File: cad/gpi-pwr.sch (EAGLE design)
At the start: 103 parts, among them CN1 HEADER-1X2, CN2 HEADER-3X1, CN3 HEADER-1X2.4, Q1 MOSFETTO247REV, Q3 MOSFETTO247REV, Q5 MOSFETTO247REV, Q6 MOSFETTO247REV, Q7 MOSFETTO247REV, Q8 MOSFETTO247REV, U1 ACS709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

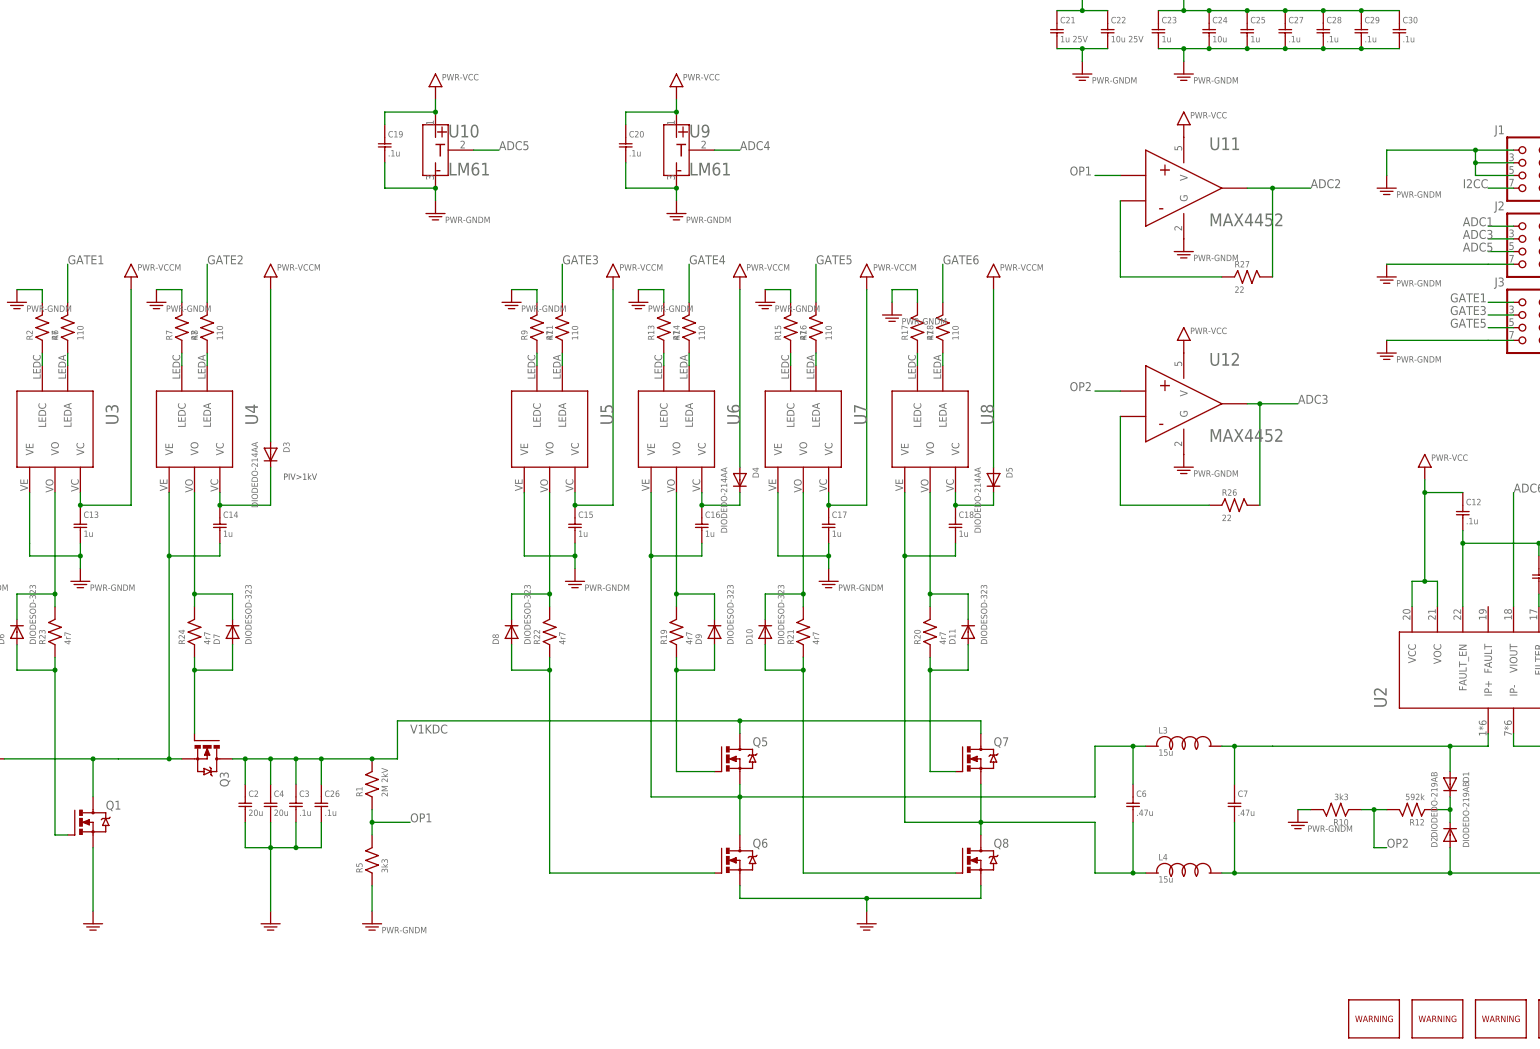
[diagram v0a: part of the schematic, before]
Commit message: output filter
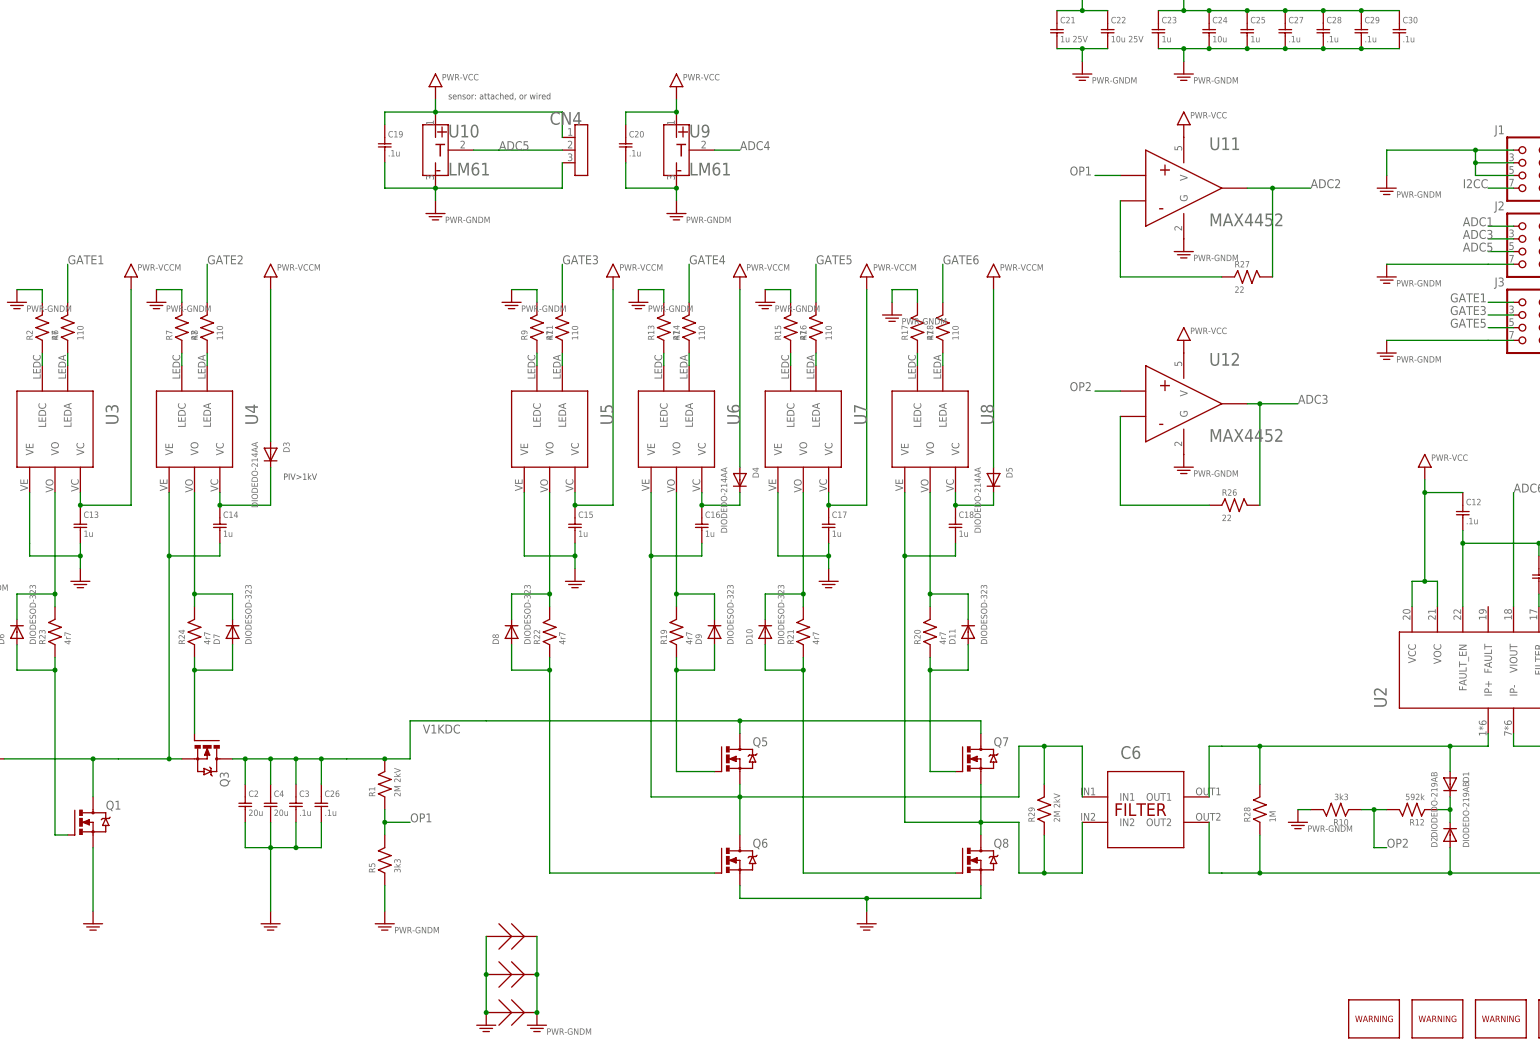
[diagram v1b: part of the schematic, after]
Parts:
- removed C7: .47u, jaw:CR46KI333000N1M
- removed L3, L4: 15u, jaw:L2303
- added CN4: HEADER-3X12MM, jaw:HEADER-3X12MM
- added R28: 1M, jaw:R1206
- added R29: 2M 2kV, jaw:R2512
- added Z1, Z2, Z3: SHORT, jaw:SHORT
- C6: value .47u -> FILTER; device jaw:CR46KI333000N1M -> jaw-brd:FILTER
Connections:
- net ADC5: now also CN4.2
- net GND: now also C13.P$2, C15.P$2, C17.P$2, U3.VE, U5.VE, U7.VE, Z1.P$1, Z2.P$1, Z3.P$1
- net GNDM: now also CN4.3, Z1.P$2, Z2.P$2, Z3.P$2; no longer C13.P$2, C15.P$2, C17.P$2, U3.VE, U5.VE, U7.VE
- net N$15: now also C6.IN1, R29.P$2; no longer C6.P$1, L3.P$1
- net N$16: now also C6.IN2, R29.P$1; no longer C6.P$2, L4.P$1
- net N$24: now also C6.OUT1, R28.P$2; no longer C7.P$1, L3.P$2
- net N$25: now also C6.OUT2, R28.P$1; no longer C7.P$2, L4.P$2
- net VCC: now also CN4.1
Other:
- note added: "sensor: attached, or wired"
- moved on the sheet: R1, R5

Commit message: tweak
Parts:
- removed R29: 2M 2kV, jaw:R2512
- removed R3: 392k, jaw:R1206
- R4: value 392k -> 1M
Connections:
- net ADC1: now also J3.P$1; no longer J2.P$1
- net ADC2: now also J3.P$2; no longer J2.P$2
- net ADC3: now also J3.P$3; no longer J2.P$3
- net ADC4: now also J3.P$4; no longer J2.P$4
- net ADC5: now also J3.P$5; no longer J2.P$5
- net ADC6: now also J3.P$6; no longer J2.P$6
- net GATE1: now also J2.P$1; no longer J3.P$1
- net GATE2: now also J2.P$2; no longer J3.P$2
- net GATE3: now also J2.P$3; no longer J3.P$3
- net GATE4: now also J2.P$4; no longer J3.P$4
- net GATE5: now also J2.P$5; no longer J3.P$5
- net GATE6: now also J2.P$6; no longer J3.P$6
- net N$11: no longer R3.P$2
- net N$15: no longer R29.P$2
- net N$16: no longer R29.P$1
- net N$25: no longer R3.P$1
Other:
- moved on the sheet: J2, J3
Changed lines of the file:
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@@
 <part name="VCC3" library="jaw" deviceset="PWR-VCC" device=""/>
 <part name="J1" library="jaw" deviceset="HEADER-2X4" device=""/>
+<part name="J3" library="jaw" deviceset="HEADER-2X4" device=""/>
 <part name="J2" library="jaw" deviceset="HEADER-2X4" device=""/>
-<part name="J3" library="jaw" deviceset="HEADER-2X4" device=""/>
 <part name="CN3" library="jaw" deviceset="HEADER-1X2" device=".4"/>
 <part name="JP1" library="adafruit" deviceset="PINHD-1X1" device=""/>
@@
 <part name="VCC4" library="jaw" deviceset="PWR-VCC" device=""/>
 <part name="VCC5" library="jaw" deviceset="PWR-VCC" device=""/>
-<part name="R3" library="jaw" deviceset="R" device="1206" value="392k"/>
-<part name="R4" library="jaw" deviceset="R" device="1206" value="392k"/>
+<part name="R4" library="jaw" deviceset="R" device="1206" value="1M"/>
 <part name="R19" library="jaw" deviceset="R" device="SMD0508" value="4r7"/>
 <part name="R20" library="jaw" deviceset="R" device="SMD0508" value="4r7"/>
@@
 <part name="Z3" library="jaw" deviceset="SHORT" device=""/>
 <part name="C6" library="jaw-brd" deviceset="FILTER" device=""/>
-<part name="R29" library="jaw" deviceset="R" device="2512" value="2M 2kV"/>
 </parts>
 <sheets>
@@
 <instance part="VCC3" gate="G$1" x="401.32" y="218.44"/>
 <instance part="J1" gate="A" x="373.38" y="213.36"/>
-<instance part="J2" gate="A" x="373.38" y="198.12"/>
-<instance part="J3" gate="A" x="373.38" y="182.88"/>
+<instance part="J3" gate="A" x="373.38" y="198.12"/>
+<instance part="J2" gate="A" x="373.38" y="182.88"/>
 <instance part="CN3" gate="G$1" x="15.24" y="71.12" rot="R180"/>
 <instance part="JP1" gate="G$1" x="391.16" y="86.36" rot="R180"/>
@@
 <instance part="VCC4" gate="G$1" x="154.94" y="231.14"/>
 <instance part="VCC5" gate="G$1" x="203.2" y="231.14"/>
-<instance part="R3" gate="G$1" x="401.32" y="81.28" rot="R90"/>
 <instance part="R4" gate="G$1" x="401.32" y="91.44" rot="R90"/>
 <instance part="R19" gate="G$1" x="203.2" y="121.92" rot="R90"/>
@@
 <instance part="Z3" gate="G$1" x="170.18" y="60.96"/>
 <instance part="C6" gate="G$1" x="297.18" y="86.36"/>
-<instance part="R29" gate="G$1" x="276.86" y="86.36" rot="R90"/>
 </instances>
 <busses>
@@
 <net name="ADC2" class="0">
 <segment>
-<pinref part="J2" gate="A" pin="P$2"/>
+<pinref part="J3" gate="A" pin="P$2"/>
 <wire x1="378.46" y1="203.2" x2="388.62" y2="203.2" width="0.1524" layer="91"/>
 <label x="388.62" y="203.2" size="1.778" layer="95"/>
@@
 <wire x1="358.14" y1="78.74" x2="358.14" y2="73.66" width="0.1524" layer="91"/>
 <junction x="358.14" y="73.66"/>
-<pinref part="R3" gate="G$1" pin="P$1"/>
-<wire x1="401.32" y1="76.2" x2="401.32" y2="73.66" width="0.1524" layer="91"/>
-<junction x="401.32" y="73.66"/>
 <wire x1="309.88" y1="73.66" x2="312.42" y2="73.66" width="0.1524" layer="91"/>
 <wire x1="312.42" y1="73.66" x2="320.04" y2="73.66" width="0.1524" layer="91"/>
@@
 </segment>
 <segment>
-<pinref part="J2" gate="A" pin="P$1"/>
+<pinref part="J3" gate="A" pin="P$1"/>
 <wire x1="370.84" y1="203.2" x2="365.76" y2="203.2" width="0.1524" layer="91"/>
 <label x="360.68" y="203.2" size="1.778" layer="95"/>
@@
 <net name="ADC4" class="0">
 <segment>
-<pinref part="J2" gate="A" pin="P$4"/>
+<pinref part="J3" gate="A" pin="P$4"/>
 <wire x1="378.46" y1="200.66" x2="388.62" y2="200.66" width="0.1524" layer="91"/>
 <label x="388.62" y="200.66" size="1.778" layer="95"/>
@@
 <wire x1="215.9" y1="88.9" x2="215.9" y2="91.44" width="0.1524" layer="91"/>
 <wire x1="215.9" y1="88.9" x2="271.78" y2="88.9" width="0.1524" layer="91"/>
-<wire x1="271.78" y1="88.9" x2="271.78" y2="99.06" width="0.1524" layer="91"/>
 <junction x="215.9" y="88.9"/>
 <wire x1="198.12" y1="137.16" x2="198.12" y2="88.9" width="0.1524" layer="91"/>
@@
 <junction x="198.12" y="137.16"/>
 <pinref part="C6" gate="G$1" pin="IN1"/>
-<wire x1="271.78" y1="99.06" x2="276.86" y2="99.06" width="0.1524" layer="91"/>
-<wire x1="276.86" y1="99.06" x2="284.48" y2="99.06" width="0.1524" layer="91"/>
-<wire x1="284.48" y1="99.06" x2="284.48" y2="88.9" width="0.1524" layer="91"/>
-<wire x1="276.86" y1="91.44" x2="276.86" y2="99.06" width="0.1524" layer="91"/>
-<junction x="276.86" y="99.06"/>
-<pinref part="R29" gate="G$1" pin="P$2"/>
+<wire x1="271.78" y1="88.9" x2="276.86" y2="88.9" width="0.1524" layer="91"/>
+<wire x1="276.86" y1="88.9" x2="284.48" y2="88.9" width="0.1524" layer="91"/>
 </segment>
 </net>
@@
 <wire x1="264.16" y1="83.82" x2="264.16" y2="91.44" width="0.1524" layer="91"/>
 <wire x1="264.16" y1="83.82" x2="271.78" y2="83.82" width="0.1524" layer="91"/>
-<wire x1="271.78" y1="83.82" x2="271.78" y2="73.66" width="0.1524" layer="91"/>
 <junction x="264.16" y="83.82"/>
 <wire x1="248.92" y1="137.16" x2="248.92" y2="83.82" width="0.1524" layer="91"/>
@@
 <junction x="248.92" y="137.16"/>
 <pinref part="C6" gate="G$1" pin="IN2"/>
-<wire x1="271.78" y1="73.66" x2="276.86" y2="73.66" width="0.1524" layer="91"/>
-<wire x1="276.86" y1="73.66" x2="284.48" y2="73.66" width="0.1524" layer="91"/>
-<wire x1="284.48" y1="73.66" x2="284.48" y2="83.82" width="0.1524" layer="91"/>
-<wire x1="276.86" y1="81.28" x2="276.86" y2="73.66" width="0.1524" layer="91"/>
-<junction x="276.86" y="73.66"/>
-<pinref part="R29" gate="G$1" pin="P$1"/>
+<wire x1="271.78" y1="83.82" x2="276.86" y2="83.82" width="0.1524" layer="91"/>
+<wire x1="276.86" y1="83.82" x2="284.48" y2="83.82" width="0.1524" layer="91"/>
 </segment>
 </net>
@@
 </segment>
 <segment>
-<pinref part="J3" gate="A" pin="P$1"/>
+<pinref part="J2" gate="A" pin="P$1"/>
 <wire x1="370.84" y1="187.96" x2="365.76" y2="187.96" width="0.1524" layer="91"/>
 <label x="358.14" y="187.96" size="1.778" layer="95"/>
@@
 </segment>
 <segment>
-<pinref part="J3" gate="A" pin="P$2"/>
+<pinref part="J2" gate="A" pin="P$2"/>
 <wire x1="378.46" y1="187.96" x2="388.62" y2="187.96" width="0.1524" layer="91"/>
 <label x="388.62" y="187.96" size="1.778" layer="95"/>
@@
 </segment>
 <segment>
-<pinref part="J3" gate="A" pin="P$3"/>
+<pinref part="J2" gate="A" pin="P$3"/>
 <wire x1="370.84" y1="185.42" x2="365.76" y2="185.42" width="0.1524" layer="91"/>
 <label x="358.14" y="185.42" size="1.778" layer="95"/>
@@
 </segment>
 <segment>
-<pinref part="J3" gate="A" pin="P$4"/>
+<pinref part="J2" gate="A" pin="P$4"/>
 <wire x1="378.46" y1="185.42" x2="388.62" y2="185.42" width="0.1524" layer="91"/>
 <label x="388.62" y="185.42" size="1.778" layer="95"/>
@@
 </segment>
 <segment>
-<pinref part="J3" gate="A" pin="P$5"/>
+<pinref part="J2" gate="A" pin="P$5"/>
 <wire x1="370.84" y1="182.88" x2="365.76" y2="182.88" width="0.1524" layer="91"/>
 <label x="358.14" y="182.88" size="1.778" layer="95"/>
@@
 </segment>
 <segment>
-<pinref part="J3" gate="A" pin="P$6"/>
+<pinref part="J2" gate="A" pin="P$6"/>
 <wire x1="378.46" y1="182.88" x2="388.62" y2="182.88" width="0.1524" layer="91"/>
 <label x="388.62" y="182.88" size="1.778" layer="95"/>
@@
 <net name="ADC5" class="0">
 <segment>
-<pinref part="J2" gate="A" pin="P$5"/>
+<pinref part="J3" gate="A" pin="P$5"/>
 <wire x1="370.84" y1="198.12" x2="365.76" y2="198.12" width="0.1524" layer="91"/>
 <label x="360.68" y="198.12" size="1.778" layer="95"/>
@@
 <net name="ADC6" class="0">
 <segment>
-<pinref part="J2" gate="A" pin="P$6"/>
+<pinref part="J3" gate="A" pin="P$6"/>
 <wire x1="378.46" y1="198.12" x2="388.62" y2="198.12" width="0.1524" layer="91"/>
 <label x="388.62" y="198.12" size="1.778" layer="95"/>
@@
 <pinref part="CN2" gate="G$1" pin="2"/>
 <wire x1="393.7" y1="86.36" x2="401.32" y2="86.36" width="0.1524" layer="91"/>
-<pinref part="R3" gate="G$1" pin="P$2"/>
 <wire x1="401.32" y1="86.36" x2="408.94" y2="86.36" width="0.1524" layer="91"/>
 <junction x="401.32" y="86.36"/>
@@
 </segment>
 <segment>
-<pinref part="J2" gate="A" pin="P$3"/>
+<pinref part="J3" gate="A" pin="P$3"/>
 <wire x1="370.84" y1="200.66" x2="365.76" y2="200.66" width="0.1524" layer="91"/>
 <label x="360.68" y="200.66" size="1.778" layer="95"/>
@@
 </segment>
 <segment>
-<pinref part="J2" gate="A" pin="P$7"/>
+<pinref part="J3" gate="A" pin="P$7"/>
 <wire x1="370.84" y1="195.58" x2="365.76" y2="195.58" width="0.1524" layer="91"/>
 <pinref part="GNDM20" gate="G$1" pin="GNDM"/>
@@
 </segment>
 <segment>
-<pinref part="J3" gate="A" pin="P$7"/>
+<pinref part="J2" gate="A" pin="P$7"/>
 <wire x1="370.84" y1="180.34" x2="365.76" y2="180.34" width="0.1524" layer="91"/>
 <pinref part="GNDM21" gate="G$1" pin="GNDM"/>
@@
 </segment>
 <segment>
-<pinref part="J3" gate="A" pin="P$8"/>
+<pinref part="J2" gate="A" pin="P$8"/>
 <wire x1="378.46" y1="180.34" x2="388.62" y2="180.34" width="0.1524" layer="91"/>
 <pinref part="GNDM22" gate="G$1" pin="GNDM"/>
@@
 </segment>
 <segment>
-<pinref part="J2" gate="A" pin="P$8"/>
+<pinref part="J3" gate="A" pin="P$8"/>
 <wire x1="378.46" y1="195.58" x2="388.62" y2="195.58" width="0.1524" layer="91"/>
 <pinref part="GNDM23" gate="G$1" pin="GNDM"/>

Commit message: comments
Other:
- note added: "H-bridge"
- note added: "output"
- note added: "output voltage sense"
- note added: "sensor: attached, or wired to cover"
- note added: "syncronous boost converter"
- note added: "to 12V buck board"
- note added: "to ctl board"
- note removed: "sensor: attached, or wired"
- note removed: "to Board 2"
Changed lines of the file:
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@@
 <?xml version="1.0" encoding="utf-8"?>
 <!DOCTYPE eagle SYSTEM "eagle.dtd">
-<eagle version="7.1.0">
+<eagle version="7.2.0">
 <drawing>
 <settings>
@@
 <setting verticaltext="up"/>
 </settings>
-<grid distance="0.1" unitdist="inch" unit="inch" style="lines" multiple="1" display="no" altdistance="0.01" altunitdist="inch" altunit="inch"/>
+<grid distance="0.1" unitdist="inch" unit="inch" style="lines" multiple="1" display="yes" altdistance="0.01" altunitdist="inch" altunit="inch"/>
 <layers>
 <layer number="1" name="Top" color="4" fill="1" visible="no" active="no"/>
@@
 <text x="124.46" y="152.4" size="1.27" layer="97">PIV&gt;1kV</text>
 <text x="7.62" y="88.9" size="1.778" layer="97">DC IN</text>
-<text x="7.62" y="63.5" size="1.778" layer="97">to Board 2</text>
+<text x="7.62" y="63.5" size="1.778" layer="97">to 12V buck board</text>
 <text x="383.54" y="91.44" size="1.778" layer="97">to chassis</text>
-<text x="157.48" y="228.6" size="1.27" layer="97">sensor: attached, or wired</text>
+<text x="139.7" y="236.22" size="1.778" layer="97">sensor: attached, or wired to cover</text>
+<text x="66.04" y="40.64" size="1.778" layer="97">syncronous boost converter</text>
+<text x="231.14" y="40.64" size="1.778" layer="97">H-bridge</text>
+<text x="408.94" y="66.04" size="1.778" layer="97">output</text>
+<text x="332.74" y="63.5" size="1.778" layer="97">output voltage sense</text>
+<text x="365.76" y="228.6" size="1.778" layer="97">to ctl board</text>
 </plain>
 <instances>

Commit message: pdfs, comments
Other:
- note added: "bus voltage sense"
- note added: "filter daughter board"
- note added: "power inverter - power board little box challenge"
- note added: "synchronous boost converter"
- note removed: "syncronous boost converter"
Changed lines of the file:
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@@
 <setting verticaltext="up"/>
 </settings>
-<grid distance="0.1" unitdist="inch" unit="inch" style="lines" multiple="1" display="yes" altdistance="0.01" altunitdist="inch" altunit="inch"/>
+<grid distance="0.1" unitdist="inch" unit="inch" style="lines" multiple="1" display="no" altdistance="0.01" altunitdist="inch" altunit="inch"/>
 <layers>
 <layer number="1" name="Top" color="4" fill="1" visible="no" active="no"/>
@@
 <text x="383.54" y="91.44" size="1.778" layer="97">to chassis</text>
 <text x="139.7" y="236.22" size="1.778" layer="97">sensor: attached, or wired to cover</text>
-<text x="66.04" y="40.64" size="1.778" layer="97">syncronous boost converter</text>
+<text x="66.04" y="40.64" size="1.778" layer="97">synchronous boost converter</text>
 <text x="231.14" y="40.64" size="1.778" layer="97">H-bridge</text>
 <text x="408.94" y="66.04" size="1.778" layer="97">output</text>
 <text x="332.74" y="63.5" size="1.778" layer="97">output voltage sense</text>
 <text x="365.76" y="228.6" size="1.778" layer="97">to ctl board</text>
+<text x="327.66" y="25.4" size="2.54" layer="94" ratio="10">power inverter - power board
+little box challenge</text>
+<text x="279.4" y="63.5" size="1.778" layer="97" ratio="10">filter daughter board</text>
+<text x="147.32" y="68.58" size="1.778" layer="97" ratio="10">bus voltage sense</text>
 </plain>
 <instances>
